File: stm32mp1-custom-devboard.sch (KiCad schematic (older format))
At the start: 3 parts, among them P1 Main Power Supply, U10 APX803D-29SRG-7

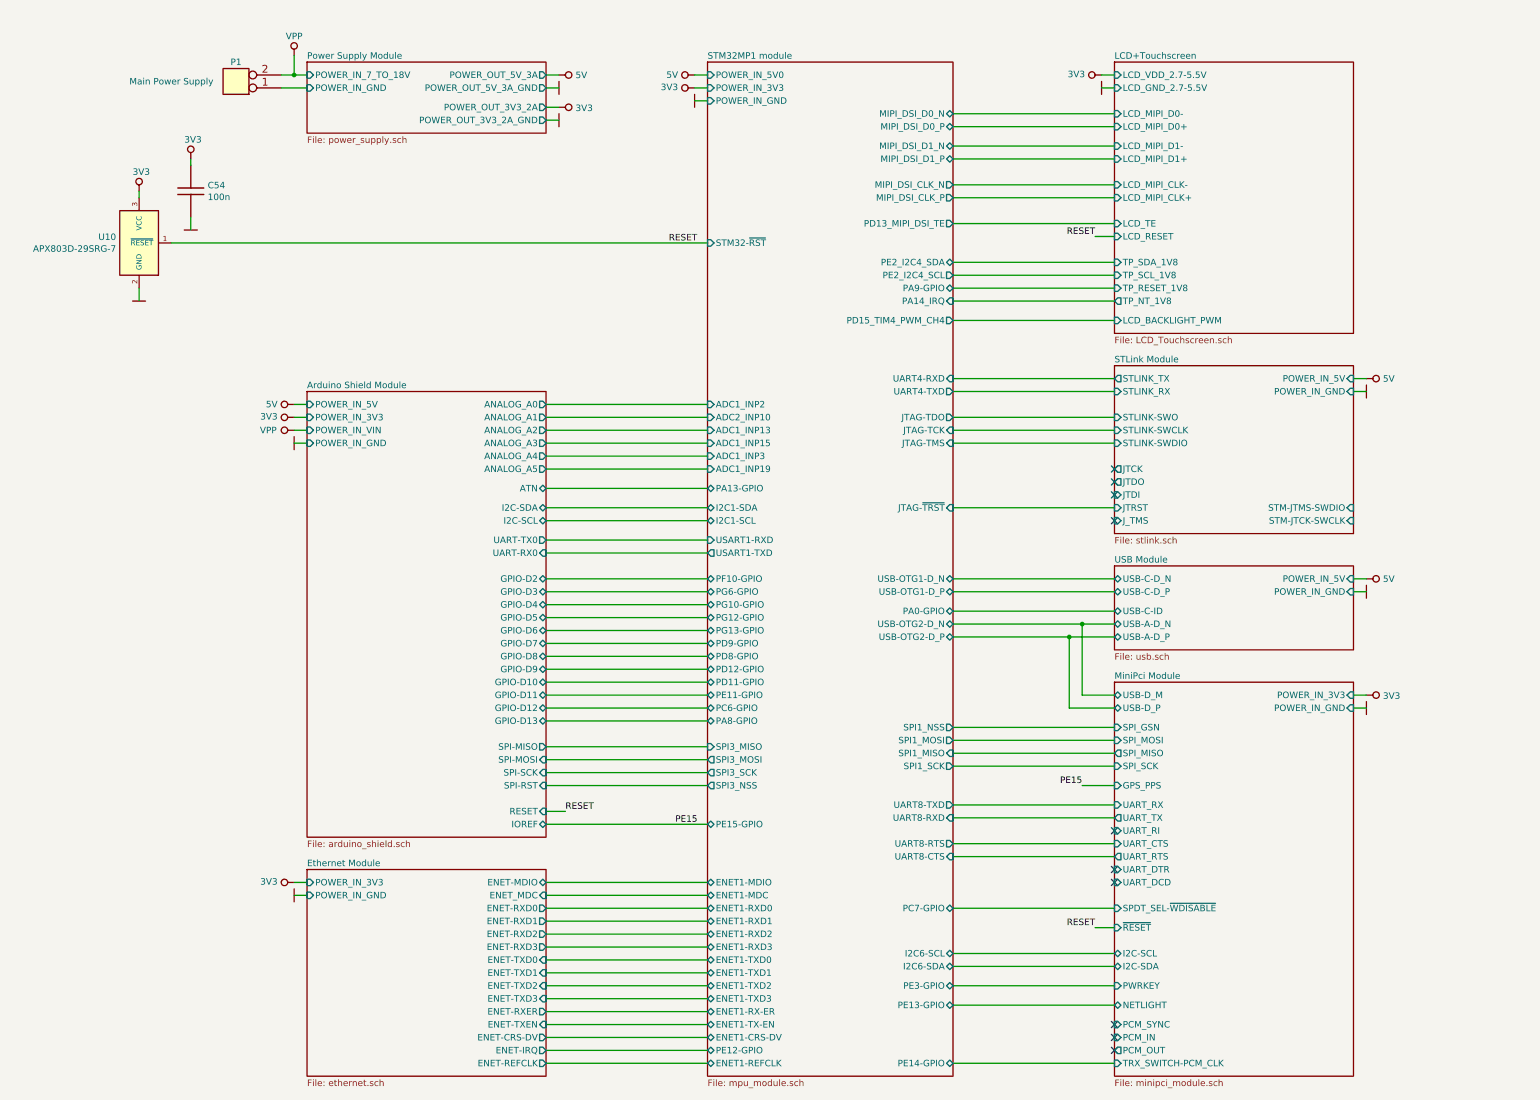
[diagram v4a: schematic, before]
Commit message: Tracking finished, started tunning
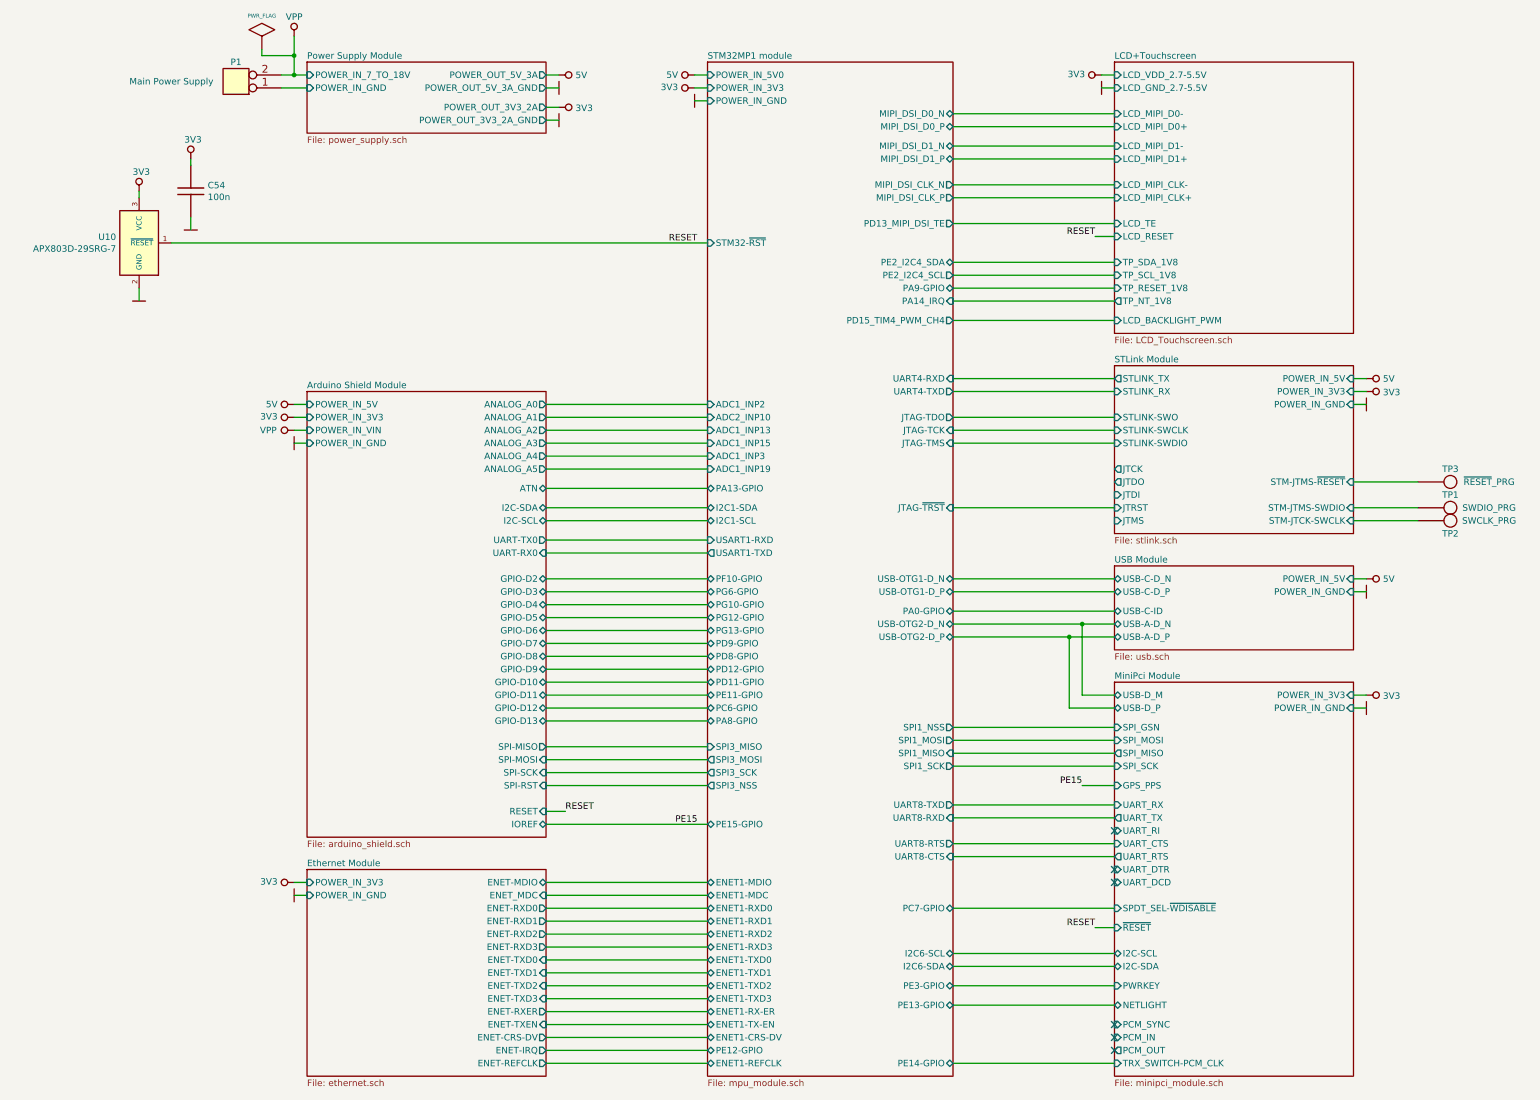
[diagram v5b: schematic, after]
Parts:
- added TP1: SWDIO_PRG, Test_Points:Test_Point_2.54mm, symbol Test_Points:Test_Point_2.54mm
- added TP2: SWCLK_PRG, Test_Points:Test_Point_2.54mm, symbol Test_Points:Test_Point_2.54mm
- added TP3: ~RESET~_PRG, Test_Points:Test_Point_2.54mm, symbol Test_Points:Test_Point_2.54mm
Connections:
- net STLink Module/STM-JTCK-SWCLK: now also TP2.1 (TP)
- net STLink Module/STM-JTMS-SWDIO: now also TP1.1 (TP)
- new net STLink Module/STM-JTMS-~RESET~: TP3.1 (TP)
- no-connect marks 10 -> 6
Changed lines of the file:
@@
 $EndComp
-Wire Wire Line
-	7400 1800 7500 1800
 Wire Wire Line
 	7500 1700 7400 1700
@@
 F27 "SPI_MISO" O L 10650 6950 50
 $EndSheet
-$Sheet
-S 10650 3950 1850 1300
-U 5FDFB166
-F0 "STLink Module" 50
-F1 "stlink.sch" 50
-F2 "POWER_IN_5V" I R 12500 4050 50
-F3 "POWER_IN_GND" I R 12500 4150 50
-F4 "STLINK_TX" O L 10650 4050 50
-F5 "JTCK" O L 10650 4750 50
-F6 "JTDO" O L 10650 4850 50
-F7 "JTDI" I L 10650 4950 50
-F8 "STLINK-SWO" I L 10650 4350 50
-F9 "STLINK-SWCLK" I L 10650 4450 50
-F10 "STLINK-SWDIO" I L 10650 4550 50
-F11 "JTRST" I L 10650 5050 50
-F12 "STM-JTMS-SWDIO" I R 12500 5050 50
-F13 "STM-JTCK-SWCLK" I R 12500 5150 50
-F14 "J_TMS" I L 10650 5150 50
-F15 "STLINK_RX" I L 10650 4150 50
-$EndSheet
 $Comp
 L Smd_Connectors:2060-452_998-404 P1
@@
 L power:GND #PWR0141
 U 1 1 60003418
-P 12600 4150
-F 0 "#PWR0141" H 12600 4250 30  0001 C CNN
-F 1 "GND" H 12600 4050 30  0001 C CNN
-F 2 "" H 12600 4150 60  0000 C CNN
-F 3 "" H 12600 4150 60  0000 C CNN
-	1    12600 4150
+P 12600 4250
+F 0 "#PWR0141" H 12600 4350 30  0001 C CNN
+F 1 "GND" H 12600 4150 30  0001 C CNN
+F 2 "" H 12600 4250 60  0000 C CNN
+F 3 "" H 12600 4250 60  0000 C CNN
+	1    12600 4250
 	0    1    1    0
 $EndComp
 Wire Wire Line
-	12500 4150 12600 4150
+	12500 4250 12600 4250
 $Comp
 L power:GND #PWR0142
@@
 L power:VPP #PWR0169
 U 1 1 601DBB64
-P 4300 1550
-F 0 "#PWR0169" H 4300 1750 40  0001 C CNN
-F 1 "VPP" H 4300 1700 50  0000 C CNN
-F 2 "" H 4300 1550 60  0000 C CNN
-F 3 "" H 4300 1550 60  0000 C CNN
-	1    4300 1550
+P 4300 1400
+F 0 "#PWR0169" H 4300 1600 40  0001 C CNN
+F 1 "VPP" H 4300 1550 50  0000 C CNN
+F 2 "" H 4300 1400 60  0000 C CNN
+F 3 "" H 4300 1400 60  0000 C CNN
+	1    4300 1400
 	1    0    0    -1
 $EndComp
@@
 Wire Wire Line
 	10650 9350 9400 9350
-NoConn ~ 10650 5150
-NoConn ~ 10650 4950
-NoConn ~ 10650 4850
-NoConn ~ 10650 4750
 Wire Wire Line
 	10650 6050 10300 6050
@@
 Wire Wire Line
 	10650 7200 10400 7200
+$Comp
+L power:PWR_FLAG #FLG0106
+U 1 1 600BF7A1
+P 4050 1500
+F 0 "#FLG0106" H 4050 1770 30  0001 C CNN
+F 1 "PWR_FLAG" H 4050 1758 30  0000 C CNN
+F 2 "" H 4050 1500 60  0000 C CNN
+F 3 "" H 4050 1500 60  0000 C CNN
+	1    4050 1500
+	1    0    0    -1
+$EndComp
+Wire Wire Line
+	4050 1500 4050 1550
+Wire Wire Line
+	4050 1550 4300 1550
+Connection ~ 4300 1550
+Wire Wire Line
+	4300 1550 4300 1400
+$Sheet
+S 10650 3950 1850 1300
+U 5FDFB166
+F0 "STLink Module" 50
+F1 "stlink.sch" 50
+F2 "POWER_IN_5V" I R 12500 4050 50
+F3 "POWER_IN_GND" I R 12500 4250 50
+F4 "STLINK_TX" O L 10650 4050 50
+F5 "JTCK" O L 10650 4750 50
+F6 "JTDO" O L 10650 4850 50
+F7 "JTDI" I L 10650 4950 50
+F8 "STLINK-SWO" I L 10650 4350 50
+F9 "STLINK-SWCLK" I L 10650 4450 50
+F10 "STLINK-SWDIO" I L 10650 4550 50
+F11 "JTRST" I L 10650 5050 50
+F12 "STM-JTMS-SWDIO" I R 12500 5050 50
+F13 "STM-JTCK-SWCLK" I R 12500 5150 50
+F14 "STLINK_RX" I L 10650 4150 50
+F15 "JTMS" I L 10650 5150 50
+F16 "POWER_IN_3V3" I R 12500 4150 50
+F17 "STM-JTMS-~RESET~" I R 12500 4850 50
+$EndSheet
+$Comp
+L power:3V3 #PWR0194
+U 1 1 6019BF14
+P 12600 4150
+F 0 "#PWR0194" H 12600 4250 40  0001 C CNN
+F 1 "3V3" V 12606 4278 50  0000 L CNN
+F 2 "" H 12600 4150 60  0000 C CNN
+F 3 "" H 12600 4150 60  0000 C CNN
+	1    12600 4150
+	0    1    1    0
+$EndComp
+Wire Wire Line
+	12600 4150 12500 4150
+Wire Wire Line
+	7500 1800 7400 1800
+$Comp
+L Test_Points:Test_Point_2.54mm TP1
+U 1 1 603189F6
+P 13250 5050
+F 0 "TP1" H 13250 4950 50  0000 C CNN
+F 1 "SWDIO_PRG" H 12950 5050 50  0000 C CNN
+F 2 "Test_Points:Test_Point_2.54mm" H 13450 4750 50  0001 C CNN
+F 3 "" H 13450 4750 50  0001 C CNN
+	1    13250 5050
+	-1   0    0    1
+$EndComp
+$Comp
+L Test_Points:Test_Point_2.54mm TP2
+U 1 1 60319569
+P 13250 5150
+F 0 "TP2" H 13250 5250 50  0000 C CNN
+F 1 "SWCLK_PRG" H 12950 5150 50  0000 C CNN
+F 2 "Test_Points:Test_Point_2.54mm" H 13450 4850 50  0001 C CNN
+F 3 "" H 13450 4850 50  0001 C CNN
+	1    13250 5150
+	-1   0    0    1
+$EndComp
+Wire Wire Line
+	13000 5150 12500 5150
+Wire Wire Line
+	12500 5050 13000 5050
+$Comp
+L Test_Points:Test_Point_2.54mm TP3
+U 1 1 6033E1FB
+P 13250 4850
+F 0 "TP3" H 13250 4750 50  0000 C CNN
+F 1 "~RESET~_PRG" H 12950 4850 50  0000 C CNN
+F 2 "Test_Points:Test_Point_2.54mm" H 13450 4550 50  0001 C CNN
+F 3 "" H 13450 4550 50  0001 C CNN
+	1    13250 4850
+	-1   0    0    1
+$EndComp
+Wire Wire Line
+	12500 4850 13000 4850
 $EndSCHEMATC

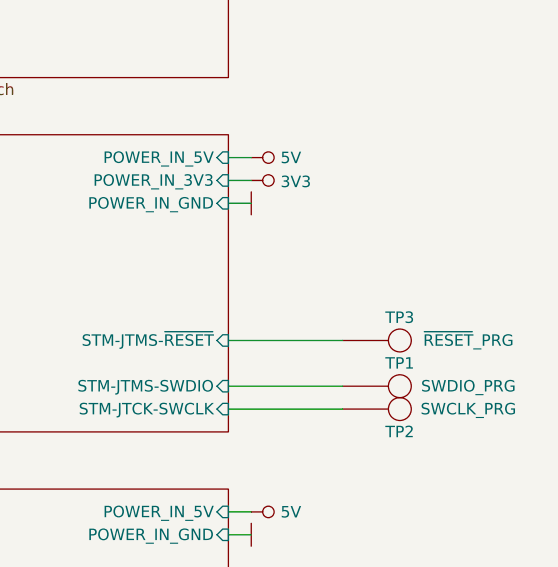
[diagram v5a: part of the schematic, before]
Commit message: Added gnd in stm32f swd interface
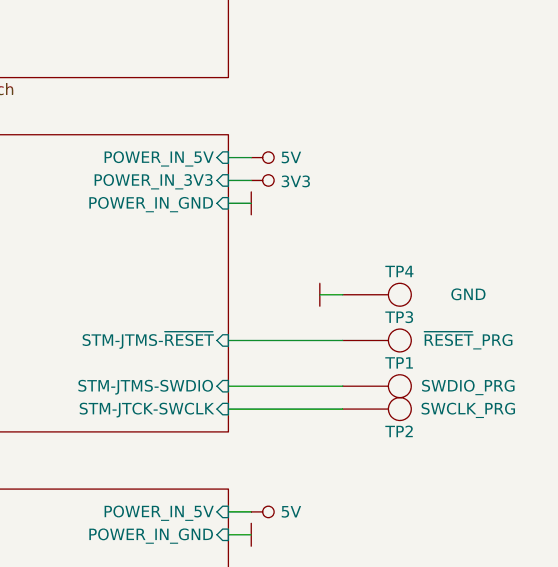
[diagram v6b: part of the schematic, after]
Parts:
- added TP4: GND, Test_Points:Test_Point_2.54mm, symbol Test_Points:Test_Point_2.54mm
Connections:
- net GND: now also TP4.1 (TP)
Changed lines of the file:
@@
 Wire Wire Line
 	12500 4850 13000 4850
+$Comp
+L Test_Points:Test_Point_2.54mm TP4
+U 1 1 600876DE
+P 13250 4650
+F 0 "TP4" H 13250 4550 50  0000 C CNN
+F 1 "GND" H 12950 4650 50  0000 C CNN
+F 2 "Test_Points:Test_Point_2.54mm" H 13450 4350 50  0001 C CNN
+F 3 "" H 13450 4350 50  0001 C CNN
+	1    13250 4650
+	-1   0    0    1
+$EndComp
+$Comp
+L power:GND #PWR0108
+U 1 1 6008F1DD
+P 12900 4650
+F 0 "#PWR0108" H 12900 4750 30  0001 C CNN
+F 1 "GND" H 12900 4550 30  0001 C CNN
+F 2 "" H 12900 4650 60  0000 C CNN
+F 3 "" H 12900 4650 60  0000 C CNN
+	1    12900 4650
+	0    -1   -1   0
+$EndComp
+Wire Wire Line
+	13000 4650 12900 4650
 $EndSCHEMATC

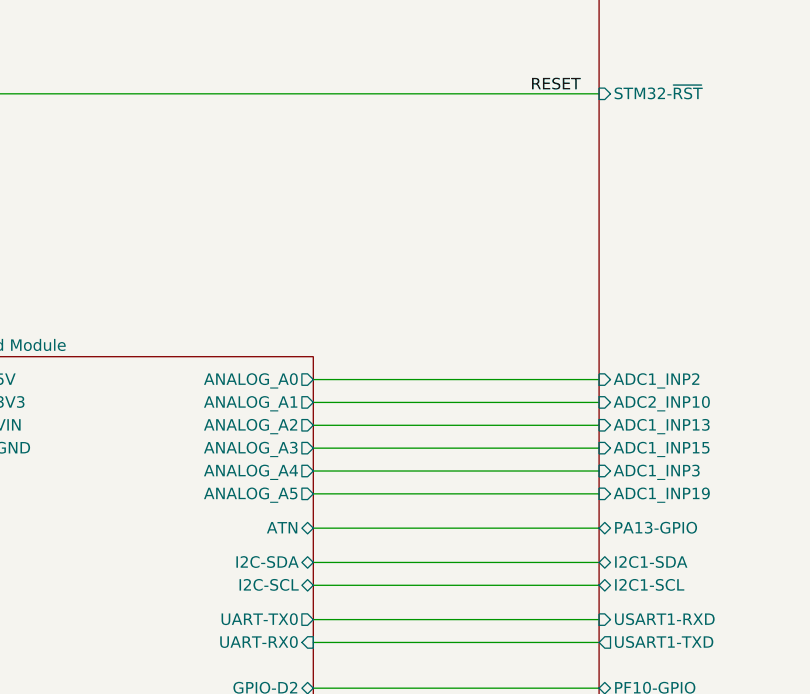
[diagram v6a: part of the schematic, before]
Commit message: Added missing components like LED diodes, i2c pull-up resistors
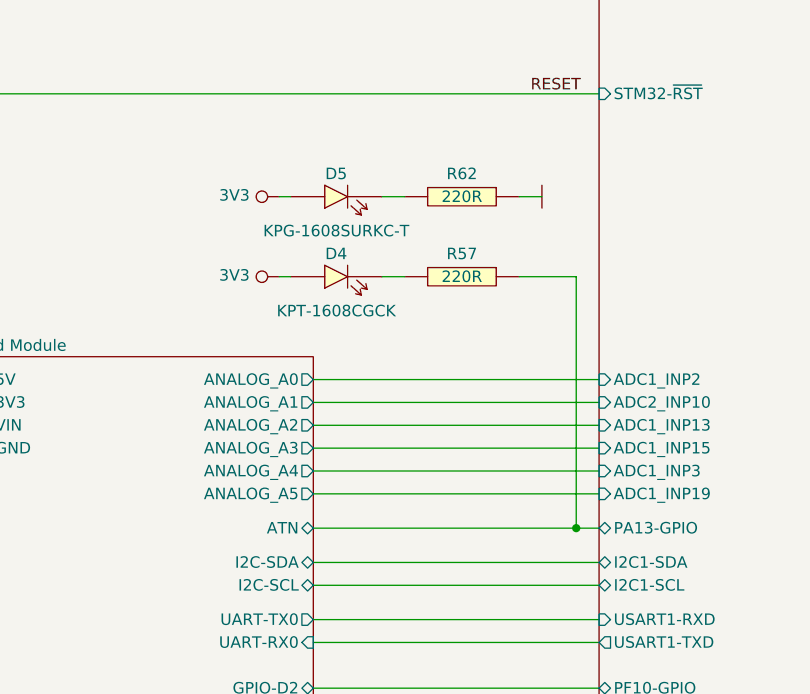
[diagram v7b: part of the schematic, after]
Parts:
- added D4: KPT-1608CGCK, Diodes:LED_KPT-1608CGCK, symbol Diodes:KPT-1608CGCK
- added D5: KPG-1608SURKC-T, Diodes:LED_KPG-1608SURKC-T, symbol Diodes:KPG-1608SURKC-T
- added R57, R62: 220R, Resistor_Smd_0603:220R_0603, symbol Resistors_Smd0603:220R
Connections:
- net 3V3: now also D4.1 (A), D5.1 (A)
- net Arduino Shield Module/ATN: now also R57.1
- net GND: now also R62.1
- new net: D4.2 (K), R57.2
- new net: D5.2 (K), R62.2
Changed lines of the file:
@@
 	6250 7950 7500 7950
 Wire Wire Line
-	6250 7500 7500 7500
-Wire Wire Line
 	6250 7200 7500 7200
 Wire Wire Line
@@
 	6250 5050 7500 5050
 Wire Wire Line
-	6250 4900 7500 4900
+	6250 4900 7400 4900
 Wire Wire Line
 	6250 4750 7500 4750
@@
 Wire Wire Line
 	13000 4650 12900 4650
+$Comp
+L Resistors_Smd0603:220R R57
+U 1 1 6009EF6C
+P 6900 3800
+F 0 "R57" V 6800 3800 50  0000 C CNN
+F 1 "220R" V 6900 3800 50  0000 C CNN
+F 2 "Resistor_Smd_0603:220R_0603" H 6900 3800 50  0001 C CNN
+F 3 "https://www.tme.eu/Document/ec37243ca557adb02ebafc5c1ab83104/CQ%20datasheet.pdf" H 6900 3800 50  0001 C CNN
+F 4 "Royal Ohm" H 6900 3800 50  0001 C CNN "Manufacturer"
+F 5 "CQ03SAF2203T5E" H 6900 3800 50  0001 C CNN "Manufacturer Part Number"
+F 6 "Tme" H 6900 3800 50  0001 C CNN "Supplier"
+F 7 "CQ0603-220K-1%" H 6900 3800 50  0001 C CNN "Supplier Part Number"
+F 8 "https://www.tme.eu/pl/details/cq0603-220k-1%25/rezystory-smd-0603/royal-ohm/cq03saf2203t5e/" H 6900 3800 50  0001 C CNN "URL"
+F 9 "0,07305" H 6900 3800 50  0001 C CNN "Price@1pc"
+F 10 "0,03414" H 6900 3800 50  0001 C CNN "Price@1000pcs"
+F 11 "MW" H 6900 3800 50  0001 C CNN "Developer"
+F 12 "0603" H 6900 3800 50  0001 C CNN "Package"
+F 13 "C103414" H 6900 3800 50  0001 C CNN "LCSC Part #(optional)"
+	1    6900 3800
+	0    1    1    0
+$EndComp
+Wire Wire Line
+	7400 4900 7400 3800
+Wire Wire Line
+	7400 3800 7150 3800
+Connection ~ 7400 4900
+Wire Wire Line
+	7400 4900 7500 4900
+Wire Wire Line
+	6250 7500 7500 7500
+Wire Wire Line
+	6650 3800 6550 3800
+$Comp
+L power:3V3 #PWR0117
+U 1 1 600C6045
+P 6100 3800
+F 0 "#PWR0117" H 6100 3900 40  0001 C CNN
+F 1 "3V3" V 6106 3928 50  0000 L CNN
+F 2 "" H 6100 3800 60  0000 C CNN
+F 3 "" H 6100 3800 60  0000 C CNN
+	1    6100 3800
+	0    -1   -1   0
+$EndComp
+Wire Wire Line
+	6150 3800 6100 3800
+$Comp
+L Resistors_Smd0603:220R R62
+U 1 1 6013BFDC
+P 6900 3450
+F 0 "R62" V 6800 3450 50  0000 C CNN
+F 1 "220R" V 6900 3450 50  0000 C CNN
+F 2 "Resistor_Smd_0603:220R_0603" H 6900 3450 50  0001 C CNN
+F 3 "https://www.tme.eu/Document/ec37243ca557adb02ebafc5c1ab83104/CQ%20datasheet.pdf" H 6900 3450 50  0001 C CNN
+F 4 "Royal Ohm" H 6900 3450 50  0001 C CNN "Manufacturer"
+F 5 "CQ03SAF2203T5E" H 6900 3450 50  0001 C CNN "Manufacturer Part Number"
+F 6 "Tme" H 6900 3450 50  0001 C CNN "Supplier"
+F 7 "CQ0603-220K-1%" H 6900 3450 50  0001 C CNN "Supplier Part Number"
+F 8 "https://www.tme.eu/pl/details/cq0603-220k-1%25/rezystory-smd-0603/royal-ohm/cq03saf2203t5e/" H 6900 3450 50  0001 C CNN "URL"
+F 9 "0,07305" H 6900 3450 50  0001 C CNN "Price@1pc"
+F 10 "0,03414" H 6900 3450 50  0001 C CNN "Price@1000pcs"
+F 11 "MW" H 6900 3450 50  0001 C CNN "Developer"
+F 12 "0603" H 6900 3450 50  0001 C CNN "Package"
+F 13 "C103414" H 6900 3450 50  0001 C CNN "LCSC Part #(optional)"
+	1    6900 3450
+	0    1    1    0
+$EndComp
+$Comp
+L Diodes:KPG-1608SURKC-T D5
+U 1 1 6013C220
+P 6350 3450
+F 0 "D5" H 6350 3550 50  0000 C CNN
+F 1 "KPG-1608SURKC-T" H 6350 3300 50  0000 C CNN
+F 2 "Diodes:LED_KPG-1608SURKC-T" H 6750 3150 50  0001 C CNN
+F 3 "https://www.tme.eu/Document/d1801a08836278504c2ab877cf18852c/KPG-1608SURKC-T.pdf" H 6750 3150 50  0001 C CNN
+F 4 "	KINGBRIGHT ELECTRONIC" H 6350 3450 50  0001 C CNN "Manufacturer"
+F 5 "KPG-1608SURKC-T" H 6350 3450 50  0001 C CNN "Manufacturer Part Number"
+F 6 "TME" H 6350 3450 50  0001 C CNN "Supplier"
+F 7 "KPG-1608SURKC-T" H 6350 3450 50  0001 C CNN "Supplier Part Number"
+F 8 "https://www.tme.eu/pl/details/kpg-1608surkc-t/diody-led-smd-kolorowe/kingbright-electronic/" H 6350 3450 50  0001 C CNN "URL"
+F 9 "0,4132" H 6350 3450 50  0001 C CNN "Price@1pc"
+F 10 "0,1995" H 6350 3450 50  0001 C CNN "Price@1000pcs"
+F 11 "WP" H 6350 3450 50  0001 C CNN "Developer"
+F 12 "0603" H 6350 3450 50  0001 C CNN "Package"
+F 13 "C192315" H 6350 3450 50  0001 C CNN "LCSC Part # (optional)"
+	1    6350 3450
+	1    0    0    -1
+$EndComp
+Wire Wire Line
+	6650 3450 6550 3450
+$Comp
+L power:3V3 #PWR0195
+U 1 1 6013C22B
+P 6100 3450
+F 0 "#PWR0195" H 6100 3550 40  0001 C CNN
+F 1 "3V3" V 6106 3578 50  0000 L CNN
+F 2 "" H 6100 3450 60  0000 C CNN
+F 3 "" H 6100 3450 60  0000 C CNN
+	1    6100 3450
+	0    -1   -1   0
+$EndComp
+Wire Wire Line
+	6150 3450 6100 3450
+$Comp
+L power:GND #PWR?
+U 1 1 601462A9
+P 7250 3450
+AR Path="/60014762/601462A9" Ref="#PWR?"  Part="1"
+AR Path="/60087A46/601462A9" Ref="#PWR?"  Part="1"
+AR Path="/601462A9" Ref="#PWR0196"  Part="1"
+F 0 "#PWR0196" H 7250 3550 30  0001 C CNN
+F 1 "GND" H 7250 3350 30  0001 C CNN
+F 2 "" H 7250 3450 60  0000 C CNN
+F 3 "" H 7250 3450 60  0000 C CNN
+	1    7250 3450
+	0    -1   -1   0
+$EndComp
+Wire Wire Line
+	7150 3450 7250 3450
+$Comp
+L Diodes:KPT-1608CGCK D4
+U 1 1 601583E3
+P 6350 3800
+F 0 "D4" H 6350 3900 50  0000 C CNN
+F 1 "KPT-1608CGCK" H 6350 3650 50  0000 C CNN
+F 2 "Diodes:LED_KPT-1608CGCK" H 6350 3800 50  0001 C CNN
+F 3 "https://www.tme.eu/Document/a39d324b494aca9bed634649dc83966d/kp-1608cgck.pdf" H 6350 3800 50  0001 C CNN
+F 4 "	KINGBRIGHT ELECTRONIC" H 6350 3800 50  0001 C CNN "Manufacturer"
+F 5 "KP-1608CGCK" H 6350 3800 50  0001 C CNN "Manufacturer Part Number"
+F 6 "TME" H 6350 3800 50  0001 C CNN "Supplier"
+F 7 "KP-1608CGCK" H 6350 3800 50  0001 C CNN "Supplier Part Number"
+F 8 "https://www.tme.eu/pl/details/kp-1608cgck/diody-led-smd-kolorowe/kingbright-electronic/" H 6350 3800 50  0001 C CNN "URL"
+F 9 "0,47368" H 6350 3800 50  0001 C CNN "Price@1pc"
+F 10 "0,16283" H 6350 3800 50  0001 C CNN "Price@1000pcs"
+F 11 "WP" H 6350 3800 50  0001 C CNN "Developer"
+F 12 "0603" H 6350 3800 50  0001 C CNN "Package"
+F 13 "C192316" H 6350 3800 50  0001 C CNN "LCSC Part # (optional)"
+	1    6350 3800
+	1    0    0    -1
+$EndComp
 $EndSCHEMATC
